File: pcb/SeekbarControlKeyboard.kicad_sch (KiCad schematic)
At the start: 16 parts, among them J1 MJ-4PP-9, J2 LED, SW1 SW_PUSH, SW2 RotaryEncoder_Switch, SW3 SW_PUSH, SW4 SW_PUSH, SW5 RESET_SW, SW6 SW_PUSH, SW7 SW_PUSH, U1 ProMicro

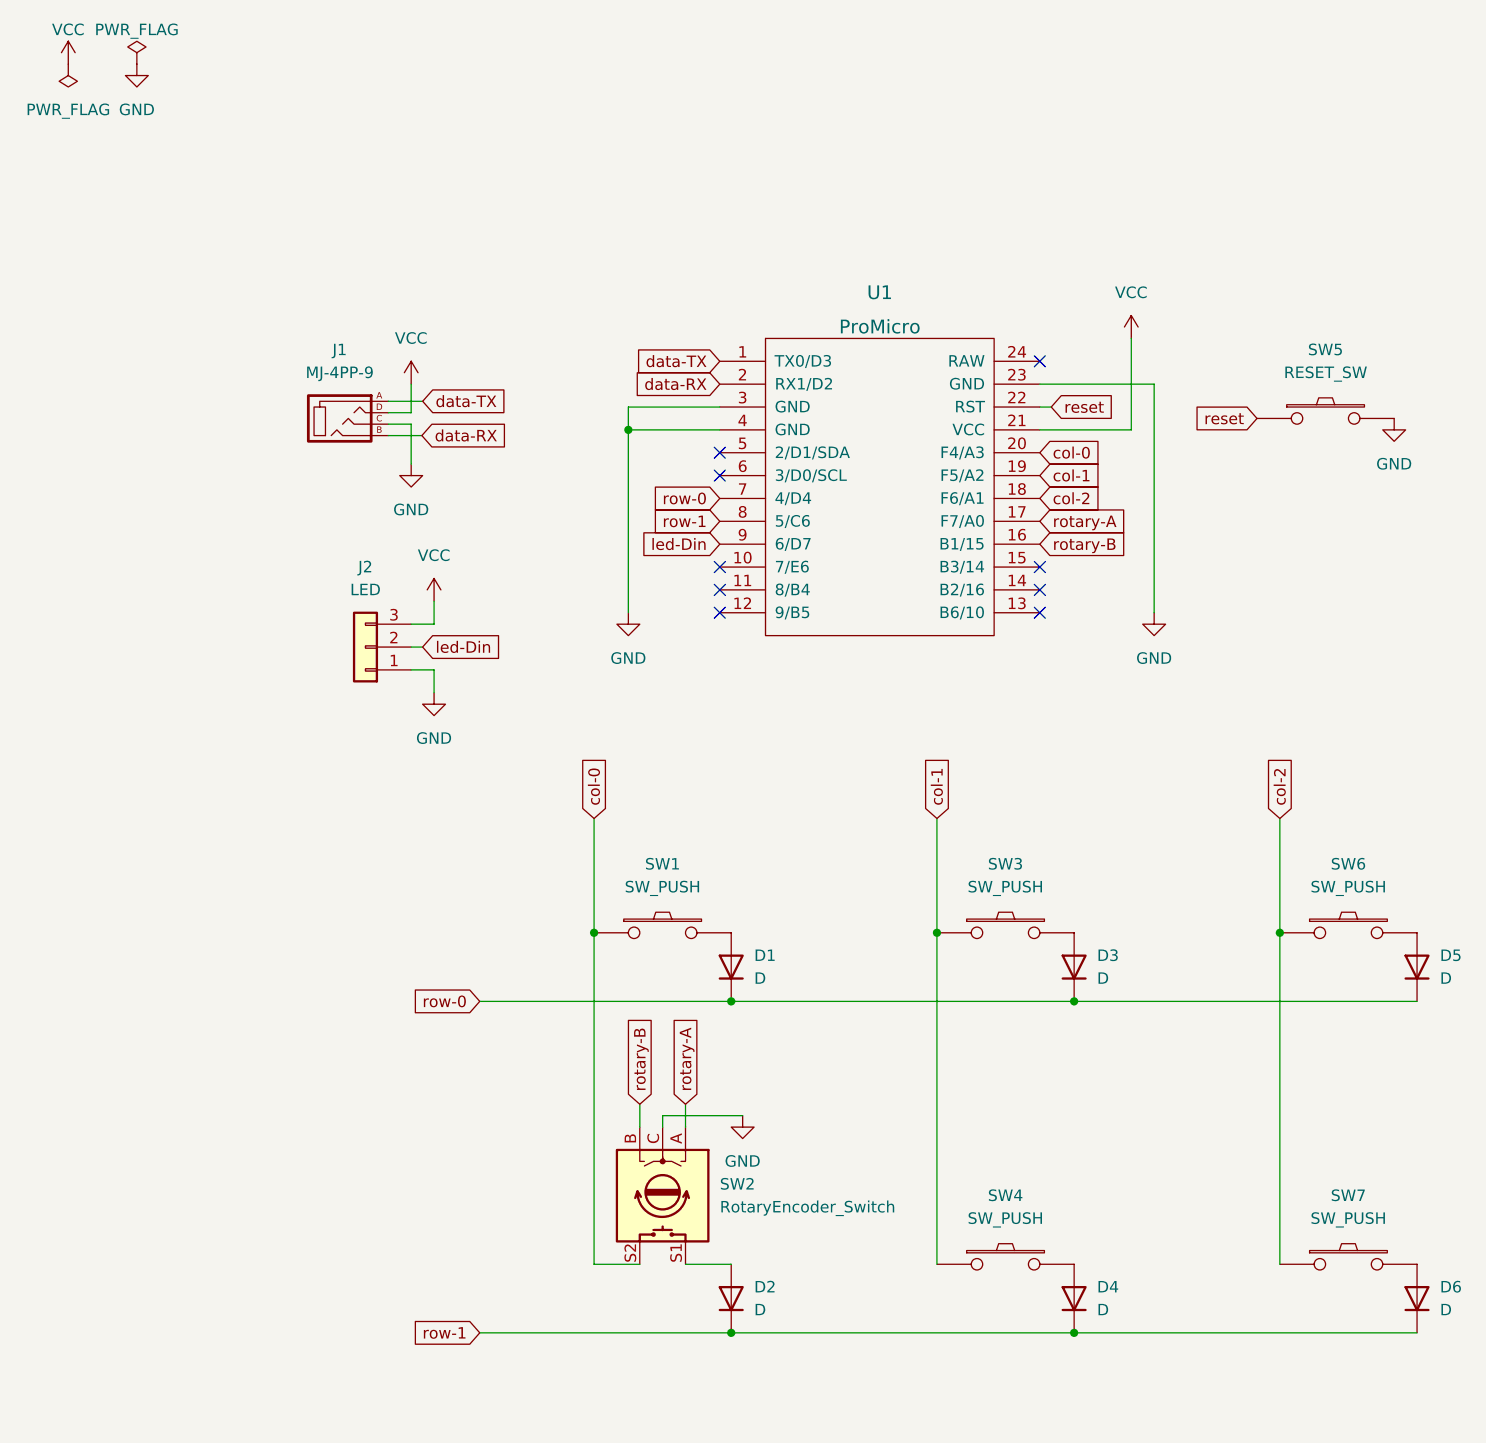
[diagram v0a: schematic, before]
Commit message: exchange rotary encoder and switch
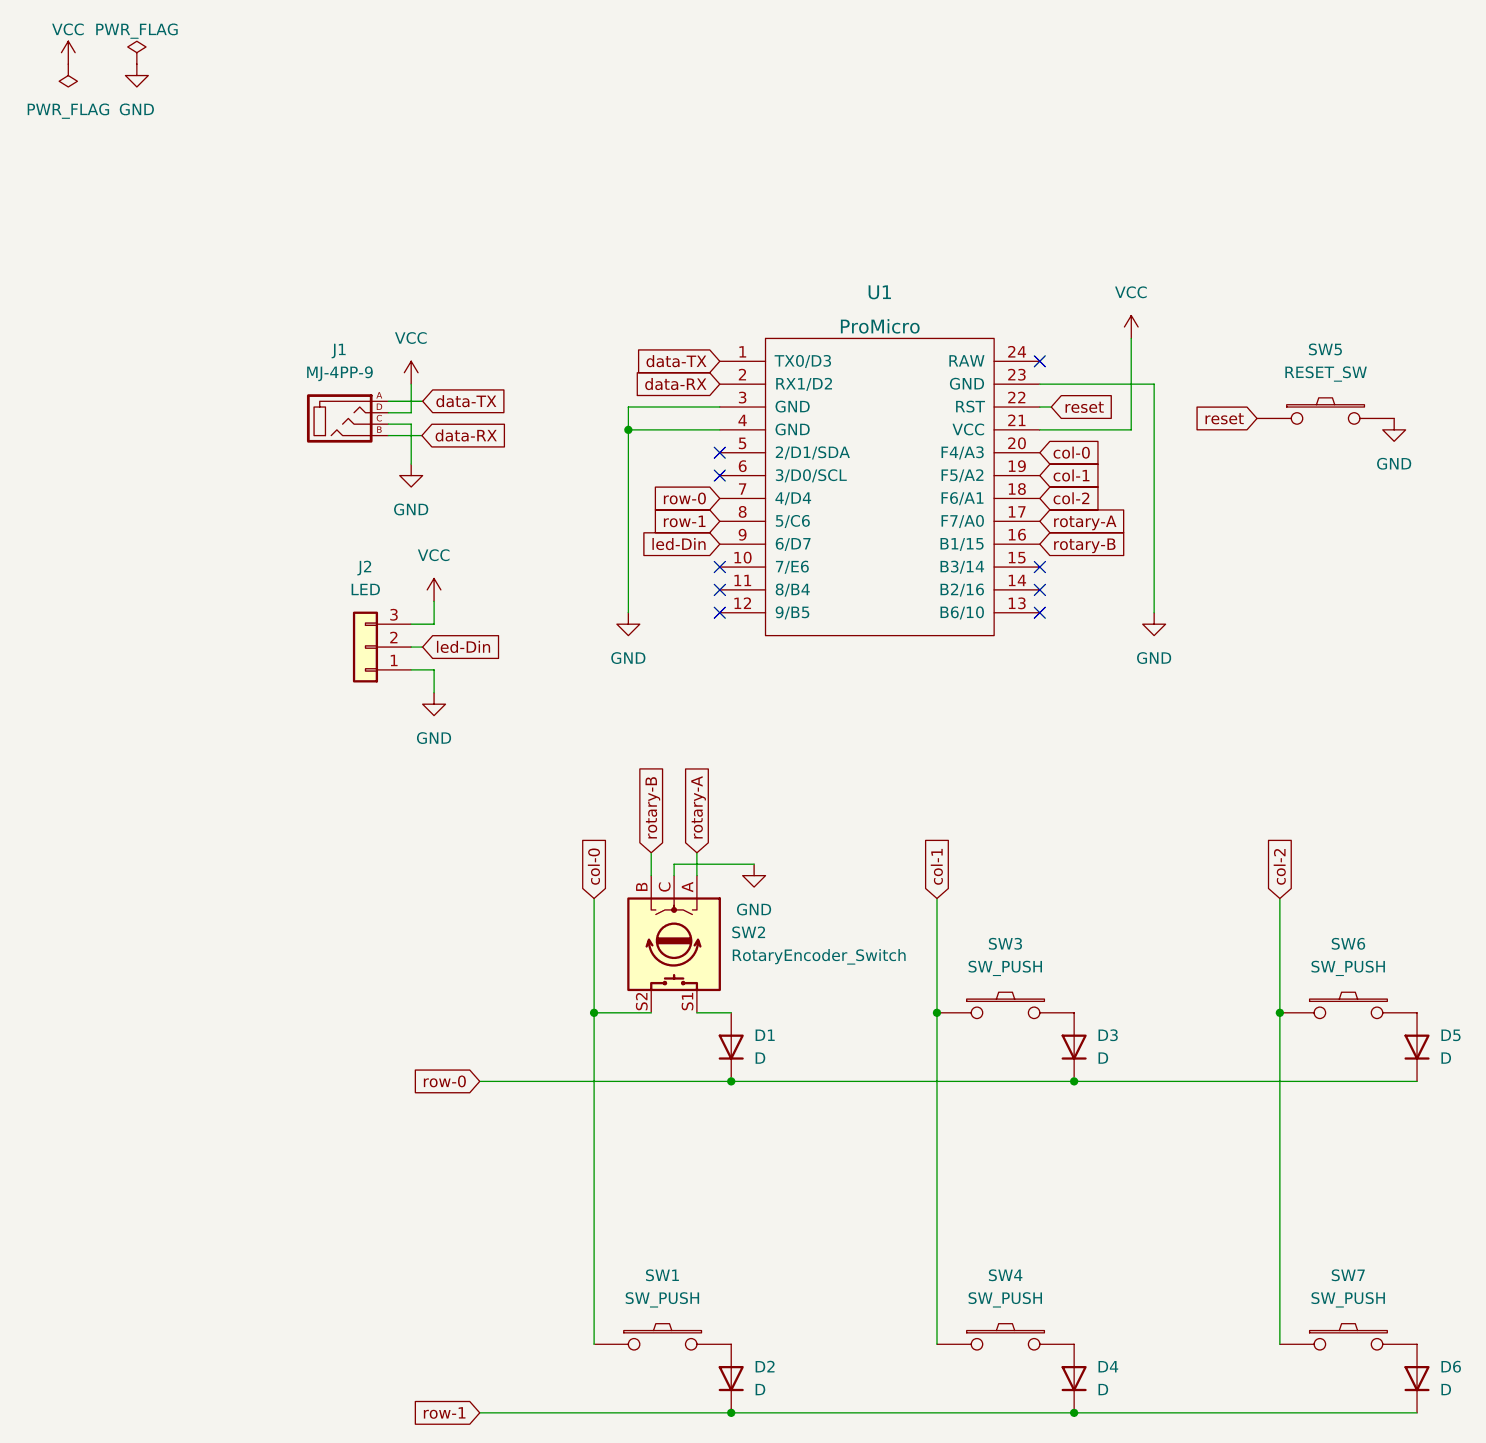
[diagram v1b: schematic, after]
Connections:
- net at D1.2 (A): now also SW2.S1; no longer SW1.2
- net at D2.2 (A): now also SW1.2; no longer SW2.S1
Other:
- moved on the sheet: D1, D2, D3, D4, D5, D6, SW1, SW2, SW3, SW4, SW6, SW7

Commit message: move folder and fix Diode fotprint close #4
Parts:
- D1, D2, D3, D4, D5, D6: footprint kbd.pretty:D3_TH_SMD_v2 -> parts:D3_TH_SMD_v3
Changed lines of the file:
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@@
       (effects (font (size 1.27 1.27)) (justify right))
     )
-    (property "Footprint" "kbd.pretty:D3_TH_SMD_v2" (id 2) (at 116.84 114.3 0)
+    (property "Footprint" "parts:D3_TH_SMD_v3" (id 2) (at 116.84 114.3 0)
       (effects (font (size 1.27 1.27)) hide)
     )
@@
       (effects (font (size 1.27 1.27)) (justify right))
     )
-    (property "Footprint" "kbd.pretty:D3_TH_SMD_v2" (id 2) (at 78.74 114.3 0)
+    (property "Footprint" "parts:D3_TH_SMD_v3" (id 2) (at 78.74 114.3 0)
       (effects (font (size 1.27 1.27)) hide)
     )
@@
       (effects (font (size 1.27 1.27)) (justify right))
     )
-    (property "Footprint" "kbd.pretty:D3_TH_SMD_v2" (id 2) (at 154.94 114.3 0)
+    (property "Footprint" "parts:D3_TH_SMD_v3" (id 2) (at 154.94 114.3 0)
       (effects (font (size 1.27 1.27)) hide)
     )
@@
       (effects (font (size 1.27 1.27)) (justify right))
     )
-    (property "Footprint" "kbd.pretty:D3_TH_SMD_v2" (id 2) (at 116.84 151.13 0)
+    (property "Footprint" "parts:D3_TH_SMD_v3" (id 2) (at 116.84 151.13 0)
       (effects (font (size 1.27 1.27)) hide)
     )
@@
       (effects (font (size 1.27 1.27)) (justify right))
     )
-    (property "Footprint" "kbd.pretty:D3_TH_SMD_v2" (id 2) (at 154.94 151.13 0)
+    (property "Footprint" "parts:D3_TH_SMD_v3" (id 2) (at 154.94 151.13 0)
       (effects (font (size 1.27 1.27)) hide)
     )
@@
       (effects (font (size 1.27 1.27)) (justify right))
     )
-    (property "Footprint" "kbd.pretty:D3_TH_SMD_v2" (id 2) (at 78.74 151.13 0)
+    (property "Footprint" "parts:D3_TH_SMD_v3" (id 2) (at 78.74 151.13 0)
       (effects (font (size 1.27 1.27)) hide)
     )
@@
     )
     (path "/098225e4-d91d-4625-a1f1-4da5feb1279e"
-      (reference "D1") (unit 1) (value "D") (footprint "kbd.pretty:D3_TH_SMD_v2")
+      (reference "D1") (unit 1) (value "D") (footprint "parts:D3_TH_SMD_v3")
     )
     (path "/dbe9ba05-a46a-4c2e-a2a8-3bab06ab2de7"
-      (reference "D2") (unit 1) (value "D") (footprint "kbd.pretty:D3_TH_SMD_v2")
+      (reference "D2") (unit 1) (value "D") (footprint "parts:D3_TH_SMD_v3")
     )
     (path "/02ec95bc-9b18-4028-a83d-b583d5fdd405"
-      (reference "D3") (unit 1) (value "D") (footprint "kbd.pretty:D3_TH_SMD_v2")
+      (reference "D3") (unit 1) (value "D") (footprint "parts:D3_TH_SMD_v3")
     )
     (path "/aa8a1b52-aefe-4354-a15a-1a02a835abd4"
-      (reference "D4") (unit 1) (value "D") (footprint "kbd.pretty:D3_TH_SMD_v2")
+      (reference "D4") (unit 1) (value "D") (footprint "parts:D3_TH_SMD_v3")
     )
     (path "/8c318120-88bf-40b3-9ae9-845435ab18ae"
-      (reference "D5") (unit 1) (value "D") (footprint "kbd.pretty:D3_TH_SMD_v2")
+      (reference "D5") (unit 1) (value "D") (footprint "parts:D3_TH_SMD_v3")
     )
     (path "/b51339ed-2880-4ea0-95e9-b26265100fe4"
-      (reference "D6") (unit 1) (value "D") (footprint "kbd.pretty:D3_TH_SMD_v2")
+      (reference "D6") (unit 1) (value "D") (footprint "parts:D3_TH_SMD_v3")
     )
     (path "/64218c02-0ded-4c54-b8b1-64f5986081d4"
